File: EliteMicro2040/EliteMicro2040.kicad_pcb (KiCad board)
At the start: 2 copper layers, 17.8 x 33 mm, 33 parts, among them J2 SKRKAEE020, U1 TLV75533PDBVR, U2 Elite-C, U3 RP2040, Y1 3225_4P

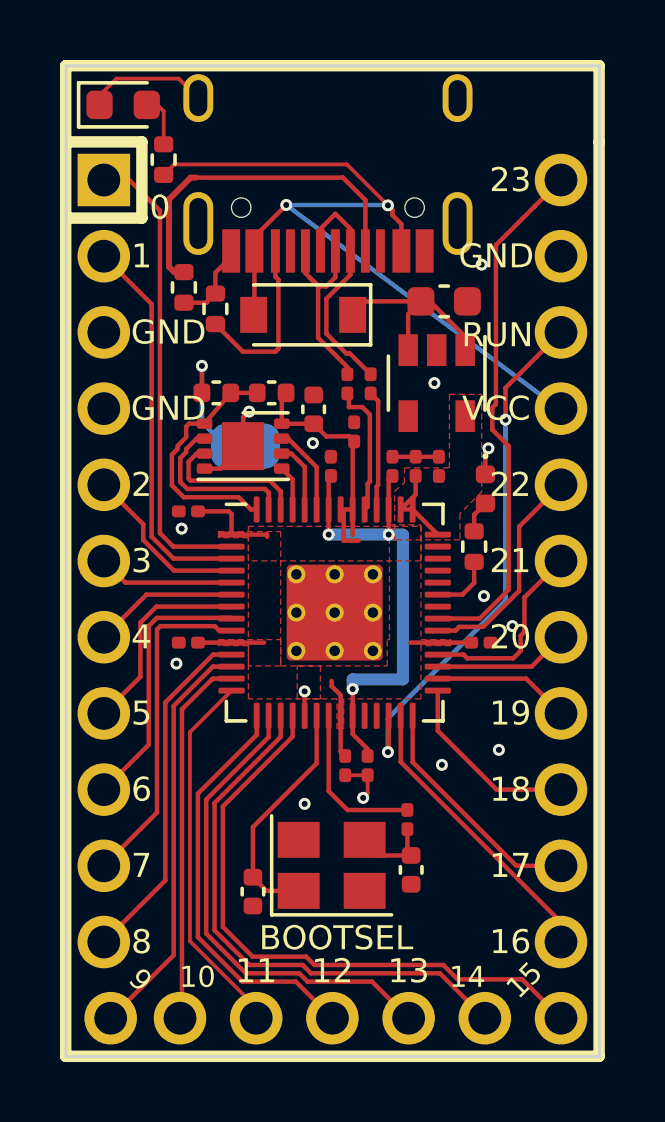
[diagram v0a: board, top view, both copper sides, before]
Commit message: moved some parts about to fit optional bypass resistor
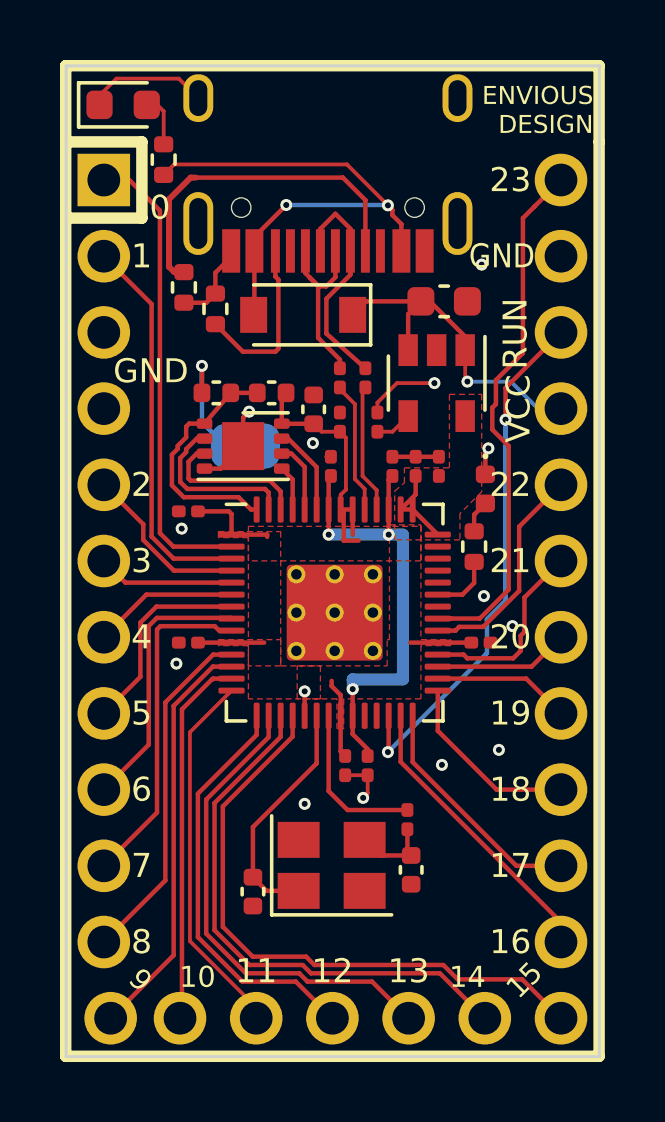
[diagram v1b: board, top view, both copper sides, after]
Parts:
- added CBP1: 10uf 0201, Capacitor_SMD:C_0201_0603Metric, F.Cu at (41.2, 35.4)
- moved C14 0.58 mm to (40.0, 35.4)
- moved R3 0.32 mm to (40.0, 33.9)
- moved R4 0.27 mm to (40.8, 33.9)
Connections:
- U2 pad 21: VBUS -> VSYS
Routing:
- net VBUS: track 28.9 -> 17.5 mm
- net VSYS: track 6.67 -> 11.3 mm, vias 0 -> 1
- net GND: track 15.0 -> 17.5 mm
- net Net-(CBP1-Pad1): track 0.00 -> 1.24 mm
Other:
- board text added: "ENVIOUS DESIGN"

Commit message: shortened pcb, added bypass resistor, pads for SPI flash and supporting decoupling capacitor
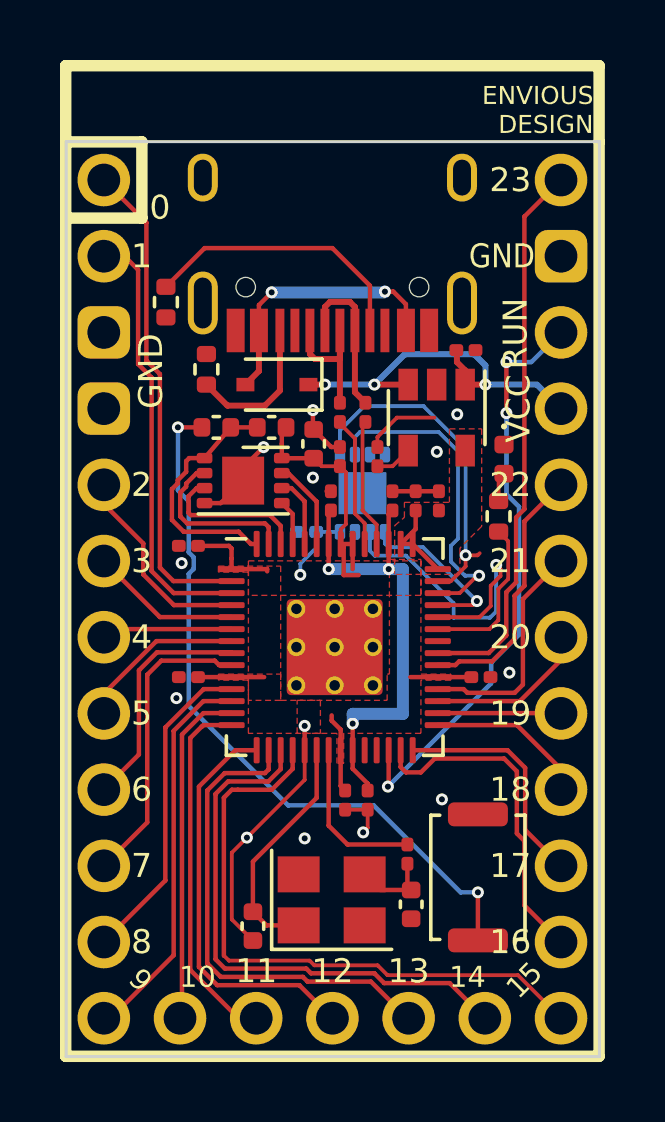
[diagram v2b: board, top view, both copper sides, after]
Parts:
- removed PWRLED1: LED_0603, LED_SMD:LED_0603_1608Metric
- removed PWRLEDRES1: 47K 0402 Resistor, Resistor_SMD:R_0402_1005Metric
- added C18: 100nf 0201, Capacitor_SMD:C_0201_0603Metric, B.Cu at (38.8, 39.0)
- added U4: W25Q32JVSS, Package_SON:SON-8-1EP_3x2mm_P0.5mm_EP1.4x1.6mm, B.Cu at (40.7, 37.7)
- C1: value 10uf 0603 6.3V -> 10uf 0201; footprint Capacitor_SMD:C_0603_1608Metric -> Capacitor_SMD:C_0201_0603Metric
- D1: footprint Diode_SMD:D_SOD-123 -> Diode_SMD:D_SOD-323
- J2: footprint Jumper:SolderJumper-2_P1.3mm_Open_RoundedPad1.0x1.5mm -> Button_Switch_SMD:SW_Push_SPST_NO_Alps_SKRK; moved to F.Cu
- moved J2 16.3 mm to (44.5, 50.5), turned to 90 degrees
- moved USB1 2.65 mm to (39.7, 24.6)
- moved D1 2.48 mm to (37.9, 34.1)
- moved R6 2.04 mm to (35.5, 33.6)
- moved C1 1.78 mm to (44.1, 33.0)
- moved GPIO25_RESISTOR1 1.30 mm to (45.2, 38.5)
- moved GPIO25_LED1 1.17 mm to (45.4, 36.6)
- moved C19 1.15 mm to (42.3, 51.5)
- moved FLASH1 1.15 mm to (36.7, 37.3)
- moved C10 1.15 mm to (42.5, 38.0)
- moved C11 1.15 mm to (43.2, 38.0)
- moved C13 1.15 mm to (40.1, 48.0)
- moved C14 1.15 mm to (40.0, 36.5)
- moved C15 1.15 mm to (34.9, 39.5)
- moved C16 1.15 mm to (34.9, 43.9)
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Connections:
- U3 pad 36: (no net) -> /GPIO24
- U3 pad 38: (no net) -> /GPIO26_ADC0
- U3 pad 39: (no net) -> /GPIO27_ADC1
- U3 pad 40: (no net) -> /GPIO28_ADC2
- U3 pad 41: (no net) -> /GPIO29_ADC3
- USB1 pad 3: (no net) -> Net-(USB1-Pad3)
- USB1 pad 9: (no net) -> Net-(USB1-Pad9)
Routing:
- net /~USB_BOOT: track 3.91 -> 24.2 mm, vias 1 -> 2
- net /GPIO29_ADC3: track 0.00 -> 11.5 mm, vias 0 -> 1
- net /GPIO26_ADC0: track 0.00 -> 11.2 mm, vias 0 -> 1
- net /GPIO28_ADC2: track 0.00 -> 10.9 mm, vias 0 -> 1
- net VBUS: track 17.5 -> 9.01 mm
- net /GPIO27_ADC1: track 0.00 -> 5.74 mm, vias 0 -> 1
- net /GPIO25: track 2.07 -> 5.36 mm
- net USB_D-: track 7.72 -> 5.26 mm
- net +3V3: track 21.6 -> 24.1 mm, vias 0 -> 1
- net Net-(R5-Pad2): track 11.7 -> 9.35 mm
- net /RUN: track 17.6 -> 19.6 mm, vias 2 -> 3
- net VSYS: track 11.3 -> 13.1 mm, vias 1 -> 3
- net Net-(PWRLED1-Pad2): track 1.79 -> 0.00 mm
- net /GPIO1: track 13.0 -> 14.5 mm
- net GND: track 17.5 -> 19.0 mm, vias 14 -> 13
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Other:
- board size 17.8 x 33 mm -> 17.8 x 30.5 mm
- board text removed: "BOOTSEL"

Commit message: Lots of changes, redid elite-c version, added more debug pads to main version and various tweaks among other things.
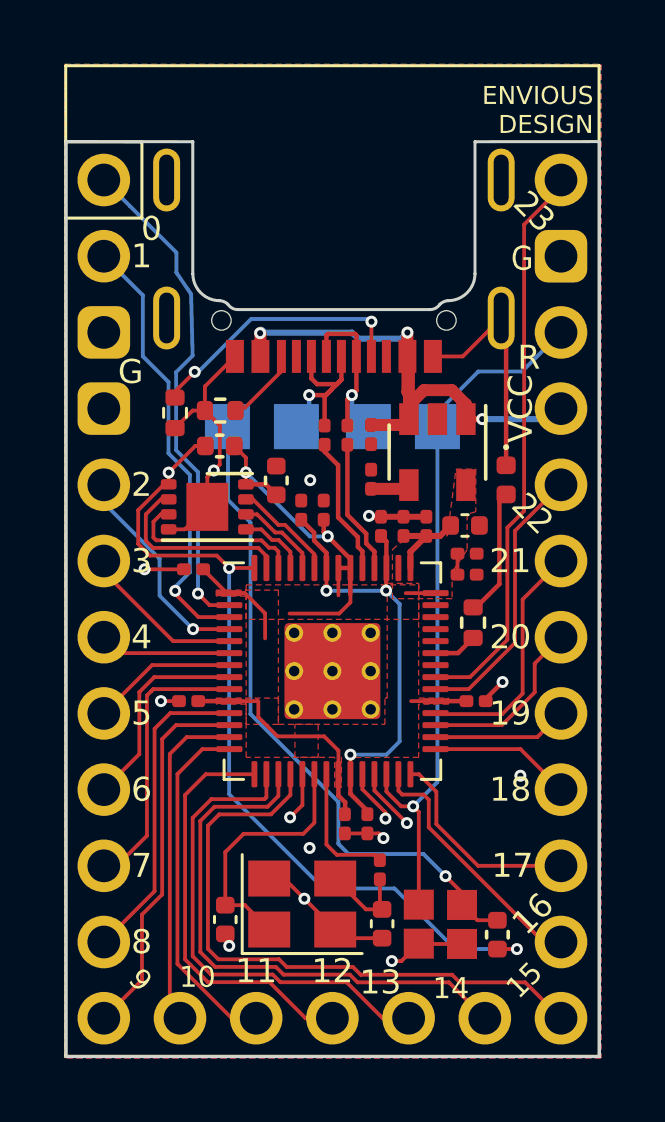
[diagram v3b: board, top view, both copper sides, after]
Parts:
- removed D1: 1N4002W, Diode_SMD:D_SOD-323
- removed U4: W25Q32JVSS, Package_SON:SON-8-1EP_3x2mm_P0.5mm_EP1.4x1.6mm
- added C4: 10uf 0402, Capacitor_SMD:C_0402_1005Metric, F.Cu at (44.1, 38.8)
- added C9: 100nf 0201, Capacitor_SMD:C_0201_0603Metric, F.Cu at (44.2, 39.8)
- added RSW1: SKRKAEE020, Jumper:SolderJumper-2_P1.3mm_Bridged_Pad1.0x1.5mm, F.Cu at (42.6, 52.1)
- added TP1: TestPoint, EnvExtras:CustomTestPoint, B.Cu at (38.5, 35.5)
- added TP2: TestPoint, EnvExtras:CustomTestPoint, B.Cu at (40.9, 35.5)
- added TP3: TestPoint, EnvExtras:CustomTestPoint, B.Cu at (43.2, 35.5)
- added TP4: TestPoint, EnvExtras:CustomTestPoint, B.Cu at (36.2, 35.5)
- C18: moved to F.Cu
- J2: footprint Button_Switch_SMD:SW_Push_SPST_NO_Alps_SKRK -> Jumper:SolderJumper-2_P1.3mm_Bridged_Pad1.0x1.5mm
- USB1: value TYPE-C-31-M-12 -> TYPE-C-31-M-14; footprint HRO-TYPE-C31-M-12:HRO-TYPE-C-31-M-12 -> josh-connectors:USB_C_TYPE-C-31-M-14
- moved R1 19.3 mm to (45.2, 52.5), turned to 90 degrees
- moved C14 9.58 mm to (34.9, 44.7), turned to 180 degrees
- moved USB1 5.70 mm to (39.8, 30.3)
- moved C18 5.54 mm to (44.2, 40.5), turned to 0 degrees
- moved C15 4.66 mm to (39.4, 38.3), turned to 90 degrees
- moved C1 4.23 mm to (41.0, 35.8), turned to 270 degrees
- moved R5 3.70 mm to (34.5, 35.1)
- moved GPIO25_RESISTOR1 3.65 mm to (44.4, 42.1)
- moved C16 3.60 mm to (35.1, 40.3)
- moved R2 1.84 mm to (35.9, 36.2)
- moved C5 1.74 mm to (37.8, 37.3)
- moved J2 1.66 mm to (44.0, 52.1), turned to 270 degrees
- moved FLASH1 1.48 mm to (35.5, 38.2)
- moved R6 1.45 mm to (36.0, 35.0), turned to 0 degrees
- moved C19 1.16 mm to (41.4, 52.1)
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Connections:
- C1 pad 1: VSYS -> VBUS
- U1 pad 1: VSYS -> VBUS
- U1 pad 3: VSYS -> VBUS
- U2 pad 21: VSYS -> VBUS
- U3 pad 36: /GPIO24 -> (no net)
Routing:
- net /QSPI_SS: track 8.20 -> 28.6 mm, vias 0 -> 3
- net VSYS: track 13.1 -> 0.00 mm, vias 3 -> 0
- net GND: track 19.0 -> 31.3 mm
- net /GPIO29_ADC3: track 11.5 -> 0.00 mm, vias 1 -> 0
- net /GPIO26_ADC0: track 11.2 -> 0.00 mm, vias 1 -> 0
- net /GPIO28_ADC2: track 10.9 -> 0.00 mm, vias 1 -> 0
- net VBUS: track 9.01 -> 18.9 mm, vias 2 -> 3
- net +3V3: track 24.1 -> 31.7 mm, vias 1 -> 2
- net /GPIO27_ADC1: track 5.74 -> 0.00 mm, vias 1 -> 0
- net /RUN: track 19.6 -> 23.7 mm, vias 3 -> 1
- net /GPIO25: track 5.36 -> 1.46 mm
- net Net-(GPIO25_LED1-Pad2): track 0.99 -> 4.28 mm
- net /GPIO16: track 11.2 -> 8.60 mm
- net Net-(R6-Pad2): track 4.95 -> 2.57 mm
- net /SWD: track 0.00 -> 2.22 mm, vias 0 -> 1
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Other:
- outline, holes or cut-outs redrawn
- board text added: "BOOT"
- board text added: "RUN"
- board text added: "USB D+"
- board text added: "USB D-"
